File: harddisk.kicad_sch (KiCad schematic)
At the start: 10 parts, among them IC45 74HCT573, IC46 74HCT573, J1 IDC 44-pin IDE

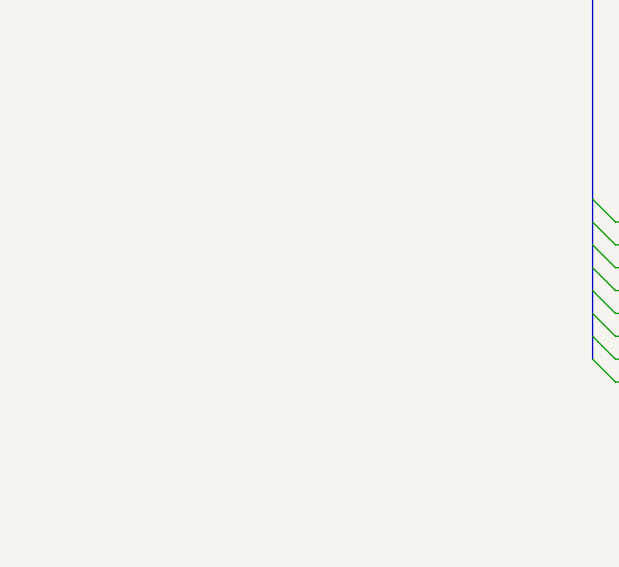
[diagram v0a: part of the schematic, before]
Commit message: complete routing
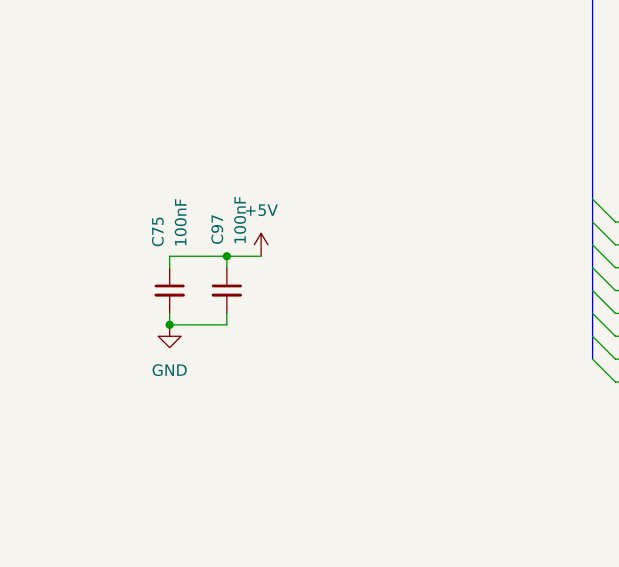
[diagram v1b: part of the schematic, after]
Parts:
- added C75, C97: 100nF, Capacitor_SMD:C_0805_2012Metric, symbol Device:C_Small
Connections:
- net +5V: now also C75.1, C97.1
- net GND: now also C75.2, C97.2
